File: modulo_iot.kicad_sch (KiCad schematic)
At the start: 13 parts, among them J3 SMA_CONNECTOR, U6 BG95-M3

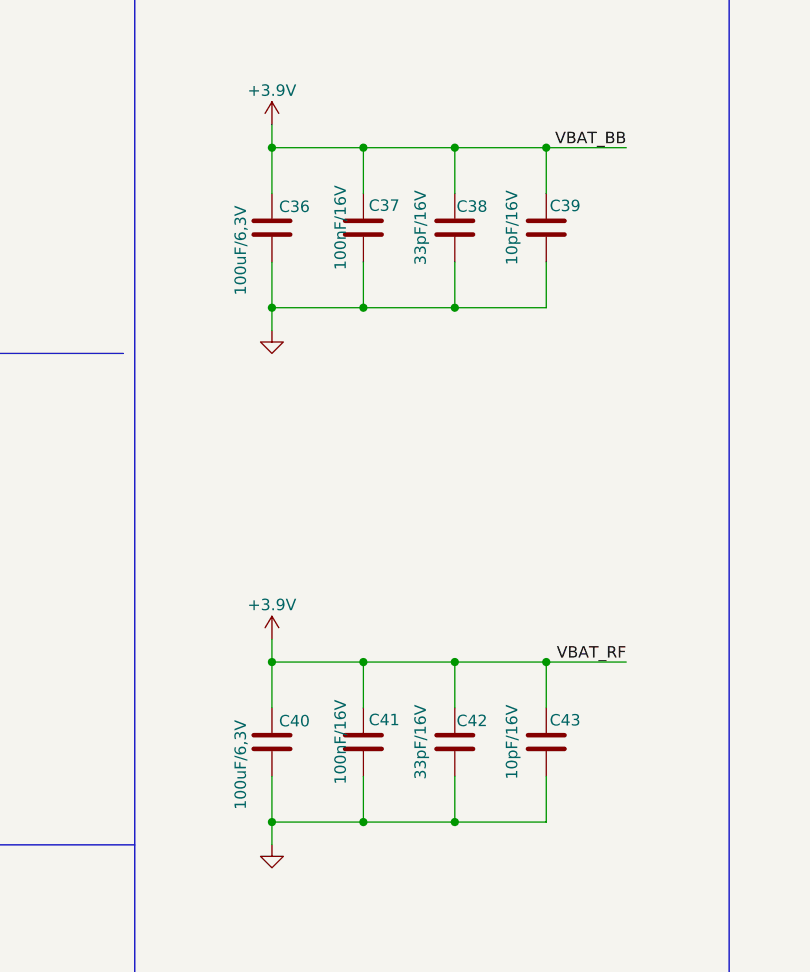
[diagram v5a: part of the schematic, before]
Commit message: Capacitores com encapsulamento 0603
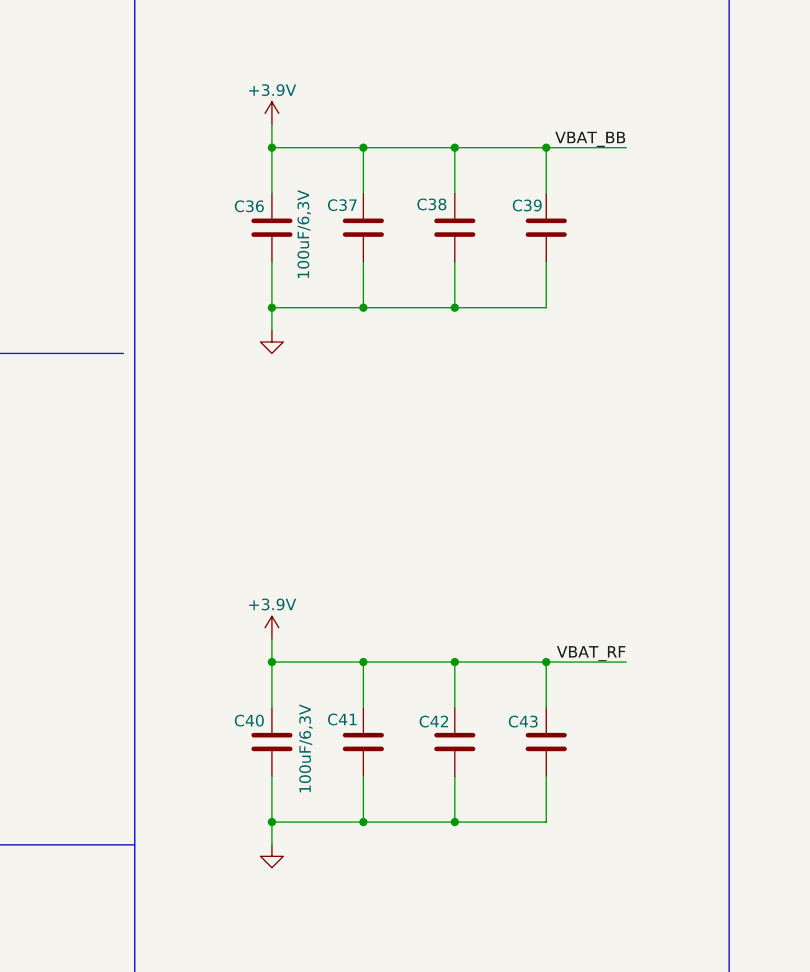
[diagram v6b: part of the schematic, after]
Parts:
- C37, C41: value 100nF/16V -> (none); footprint Capacitor_SMD:C_0402_1005Metric_Pad0.74x0.62mm_HandSolder -> (none)
- C38, C42: value 33pF/16V -> (none); footprint Capacitor_SMD:C_0402_1005Metric_Pad0.74x0.62mm_HandSolder -> (none)
- C39, C43: value 10pF/16V -> (none); footprint Capacitor_SMD:C_0402_1005Metric_Pad0.74x0.62mm_HandSolder -> (none)
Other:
- moved on the sheet: C37, C38, C39, C41, C42, C43
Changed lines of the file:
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@@
     (pin "1")
   )
-  (symbol (lib_id "Device:C") (at 146.05 115.57 180) (unit 1)
-    (in_bom yes) (on_board yes)
-    (property "Reference" "C42" (id 0) (at 147.9597 113.2135 0))
-    (property "Value" "33pF/16V" (id 1) (at 142.24 115.57 90))
-    (property "Footprint" "Capacitor_SMD:C_0402_1005Metric_Pad0.74x0.62mm_HandSolder" (id 2) (at 145.0848 111.76 0)
+  (symbol (lib_id "Device:C") (at 146.05 115.57 0) (mirror x) (unit 1)
+    (in_bom yes) (on_board yes)
+    (property "Reference" "C42" (id 0) (at 143.7582 113.3423 0))
+    (property "Value" "" (id 1) (at 149.543 115.6308 90))
+    (property "Footprint" "" (id 2) (at 147.0152 111.76 0)
       (effects (font (size 1.27 1.27)) hide)
     )
@@
     (pin "2")
   )
-  (symbol (lib_id "Device:C") (at 125.73 58.42 0) (unit 1)
-    (in_bom yes) (on_board yes)
-    (property "Reference" "C36" (id 0) (at 126.5155 56.0886 0)
+  (symbol (lib_id "Device:C") (at 125.73 58.42 0) (mirror y) (unit 1)
+    (in_bom yes) (on_board yes)
+    (property "Reference" "C36" (id 0) (at 124.9445 56.0886 0)
       (effects (font (size 1.27 1.27)) (justify left))
     )
-    (property "Value" "100uF/6,3V" (id 1) (at 122.2519 65.9392 90)
+    (property "Value" "100uF/6,3V" (id 1) (at 129.2704 64.2006 90)
       (effects (font (size 1.27 1.27)) (justify left))
     )
-    (property "Footprint" "Capacitor_SMD:C_1206_3216Metric_Pad1.33x1.80mm_HandSolder" (id 2) (at 126.6952 62.23 0)
+    (property "Footprint" "Capacitor_SMD:C_1206_3216Metric_Pad1.33x1.80mm_HandSolder" (id 2) (at 124.7648 62.23 0)
       (effects (font (size 1.27 1.27)) hide)
     )
@@
     (pin "2")
   )
-  (symbol (lib_id "Device:C") (at 125.73 115.57 0) (unit 1)
-    (in_bom yes) (on_board yes)
-    (property "Reference" "C40" (id 0) (at 126.5155 113.2386 0)
+  (symbol (lib_id "Device:C") (at 125.73 115.57 0) (mirror y) (unit 1)
+    (in_bom yes) (on_board yes)
+    (property "Reference" "C40" (id 0) (at 124.9445 113.2386 0)
       (effects (font (size 1.27 1.27)) (justify left))
     )
-    (property "Value" "100uF/6,3V" (id 1) (at 122.2519 123.0892 90)
+    (property "Value" "100uF/6,3V" (id 1) (at 129.4653 121.352 90)
       (effects (font (size 1.27 1.27)) (justify left))
     )
-    (property "Footprint" "Capacitor_SMD:C_1206_3216Metric_Pad1.33x1.80mm_HandSolder" (id 2) (at 126.6952 119.38 0)
+    (property "Footprint" "Capacitor_SMD:C_1206_3216Metric_Pad1.33x1.80mm_HandSolder" (id 2) (at 124.7648 119.38 0)
       (effects (font (size 1.27 1.27)) hide)
     )
@@
     (pin "2")
   )
-  (symbol (lib_id "Device:C") (at 156.21 58.42 180) (unit 1)
-    (in_bom yes) (on_board yes)
-    (property "Reference" "C39" (id 0) (at 158.3076 55.9943 0))
-    (property "Value" "10pF/16V" (id 1) (at 152.4 58.42 90))
-    (property "Footprint" "Capacitor_SMD:C_0402_1005Metric_Pad0.74x0.62mm_HandSolder" (id 2) (at 155.2448 54.61 0)
+  (symbol (lib_id "Device:C") (at 156.21 58.42 0) (mirror x) (unit 1)
+    (in_bom yes) (on_board yes)
+    (property "Reference" "C39" (id 0) (at 154.1124 55.9943 0))
+    (property "Value" "" (id 1) (at 159.5928 58.4158 90))
+    (property "Footprint" "" (id 2) (at 157.1752 54.61 0)
       (effects (font (size 1.27 1.27)) hide)
     )
@@
     (pin "1")
   )
-  (symbol (lib_id "Device:C") (at 135.89 58.42 180) (unit 1)
-    (in_bom yes) (on_board yes)
-    (property "Reference" "C37" (id 0) (at 138.2001 55.9597 0))
-    (property "Value" "100nF/16V" (id 1) (at 133.35 58.42 90))
-    (property "Footprint" "Capacitor_SMD:C_0402_1005Metric_Pad0.74x0.62mm_HandSolder" (id 2) (at 134.9248 54.61 0)
+  (symbol (lib_id "Device:C") (at 135.89 58.42 0) (mirror x) (unit 1)
+    (in_bom yes) (on_board yes)
+    (property "Reference" "C37" (id 0) (at 133.5799 55.9597 0))
+    (property "Value" "" (id 1) (at 139.4414 58.5429 90))
+    (property "Footprint" "" (id 2) (at 136.8552 54.61 0)
       (effects (font (size 1.27 1.27)) hide)
     )
@@
     (pin "2")
   )
-  (symbol (lib_id "Device:C") (at 156.21 115.57 180) (unit 1)
-    (in_bom yes) (on_board yes)
-    (property "Reference" "C43" (id 0) (at 158.3076 113.1443 0))
-    (property "Value" "10pF/16V" (id 1) (at 152.4 115.57 90))
-    (property "Footprint" "Capacitor_SMD:C_0402_1005Metric_Pad0.74x0.62mm_HandSolder" (id 2) (at 155.2448 111.76 0)
+  (symbol (lib_id "Device:C") (at 156.21 115.57 0) (mirror x) (unit 1)
+    (in_bom yes) (on_board yes)
+    (property "Reference" "C43" (id 0) (at 153.675 113.3423 0))
+    (property "Value" "" (id 1) (at 159.5233 115.6308 90))
+    (property "Footprint" "" (id 2) (at 157.1752 111.76 0)
       (effects (font (size 1.27 1.27)) hide)
     )
@@
     (pin "1")
   )
-  (symbol (lib_id "Device:C") (at 146.05 58.42 180) (unit 1)
-    (in_bom yes) (on_board yes)
-    (property "Reference" "C38" (id 0) (at 147.9597 56.0635 0))
-    (property "Value" "33pF/16V" (id 1) (at 142.24 58.42 90))
-    (property "Footprint" "Capacitor_SMD:C_0402_1005Metric_Pad0.74x0.62mm_HandSolder" (id 2) (at 145.0848 54.61 0)
+  (symbol (lib_id "Device:C") (at 146.05 58.42 0) (mirror x) (unit 1)
+    (in_bom yes) (on_board yes)
+    (property "Reference" "C38" (id 0) (at 143.51 55.88 0))
+    (property "Value" "" (id 1) (at 149.4853 58.5429 90))
+    (property "Footprint" "" (id 2) (at 147.0152 54.61 0)
       (effects (font (size 1.27 1.27)) hide)
     )
@@
     (pin "2")
   )
-  (symbol (lib_id "Device:C") (at 135.89 115.57 180) (unit 1)
-    (in_bom yes) (on_board yes)
-    (property "Reference" "C41" (id 0) (at 138.2001 113.1097 0))
-    (property "Value" "100nF/16V" (id 1) (at 133.35 115.57 90))
-    (property "Footprint" "Capacitor_SMD:C_0402_1005Metric_Pad0.74x0.62mm_HandSolder" (id 2) (at 134.9248 111.76 0)
-      (effects (font (size 1.27 1.27)) hide)
-    )
+  (symbol (lib_id "Device:C") (at 135.89 115.57 0) (mirror x) (unit 1)
+    (in_bom yes) (on_board yes)
+    (property "Reference" "C41" (id 0) (at 133.5799 113.1097 0))
+    (property "Value" "" (id 1) (at 139.1177 115.6308 90))
+    (property "Footprint" "" (id 2) (at 136.8552 111.76 0)
+      (effects (font (size 1.27 1.27)) hide)
+    )

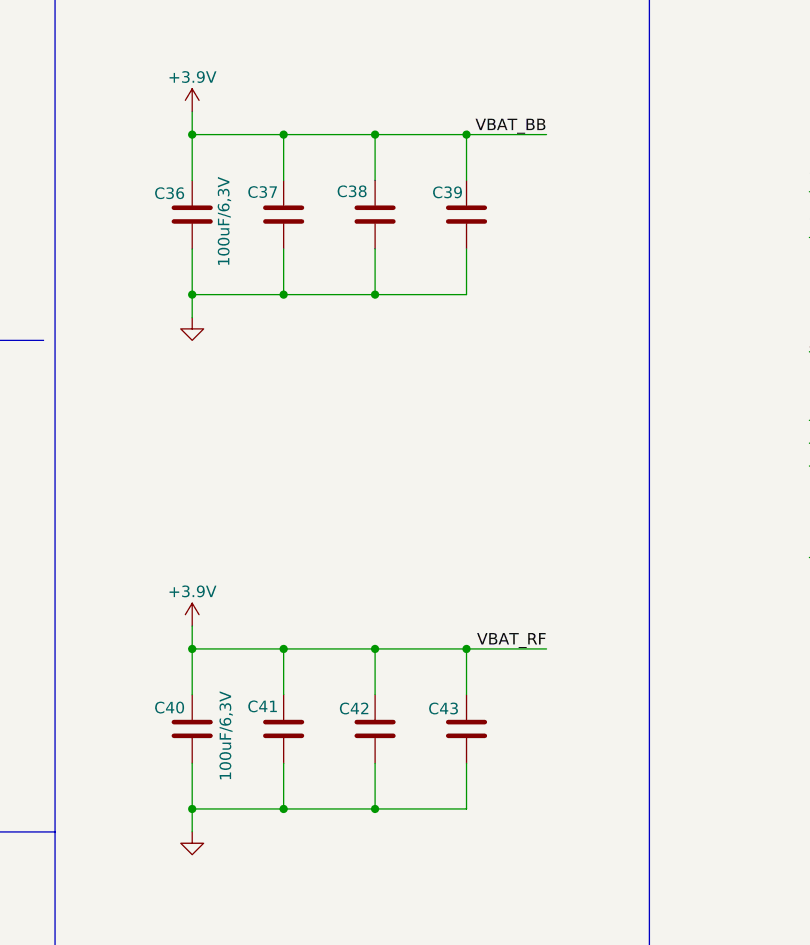
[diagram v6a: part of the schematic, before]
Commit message: Adicionado os pads dos Test Point e alterado o Bead
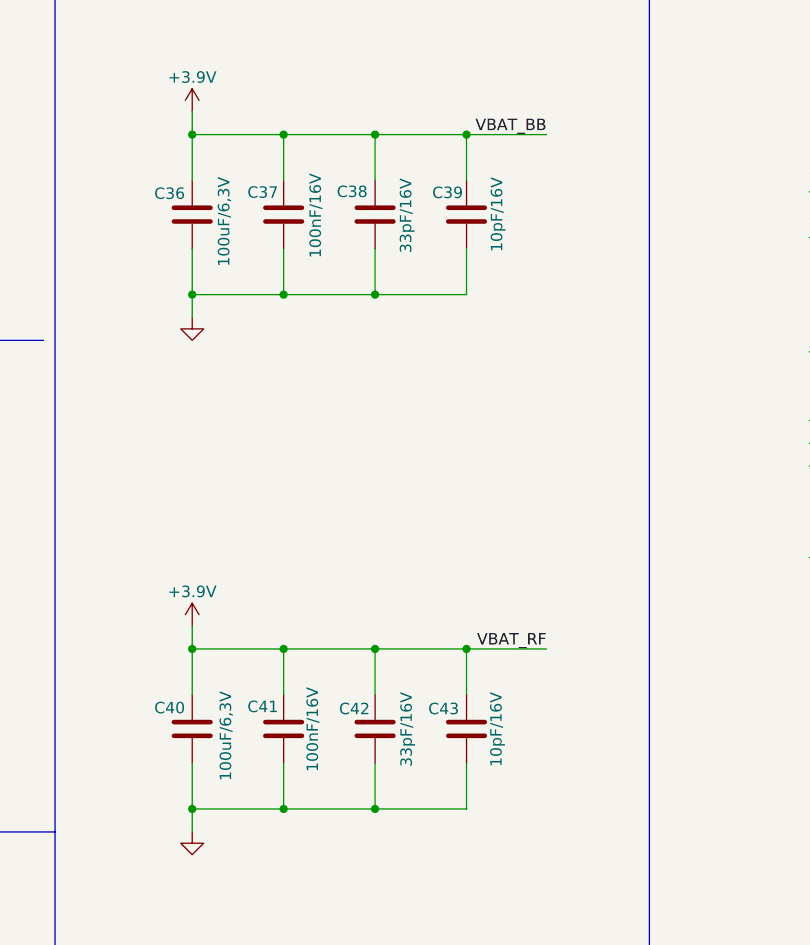
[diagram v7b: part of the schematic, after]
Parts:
- C37, C41: value (none) -> 100nF/16V; footprint (none) -> Capacitor_SMD:C_0603_1608Metric_Pad1.08x0.95mm_HandSolder
- C38, C42: value (none) -> 33pF/16V; footprint (none) -> Capacitor_SMD:C_0603_1608Metric_Pad1.08x0.95mm_HandSolder
- C39, C43: value (none) -> 10pF/16V; footprint (none) -> Capacitor_SMD:C_0603_1608Metric_Pad1.08x0.95mm_HandSolder
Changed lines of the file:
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@@
   (symbol (lib_id "Alexandre_Library:Power") (at 147.32 162.56 0) (unit 1)
     (in_bom yes) (on_board yes)
-    (property "Reference" "#PWR99" (id 0) (at 147.32 154.94 0)
+    (property "Reference" "#PWR100" (id 0) (at 147.32 154.94 0)
       (effects (font (size 1.27 1.27)) hide)
     )
@@
   (symbol (lib_id "power:GND") (at 255.27 151.13 0) (unit 1)
     (in_bom yes) (on_board yes) (fields_autoplaced)
-    (property "Reference" "#PWR097" (id 0) (at 255.27 157.48 0)
+    (property "Reference" "#PWR098" (id 0) (at 255.27 157.48 0)
       (effects (font (size 1.27 1.27)) hide)
     )
@@
   (symbol (lib_id "power:GND") (at 125.73 127 0) (mirror y) (unit 1)
     (in_bom yes) (on_board yes) (fields_autoplaced)
-    (property "Reference" "#PWR094" (id 0) (at 125.73 133.35 0)
+    (property "Reference" "#PWR095" (id 0) (at 125.73 133.35 0)
       (effects (font (size 1.27 1.27)) hide)
     )
@@
   (symbol (lib_id "power:GND") (at 139.7 170.18 0) (unit 1)
     (in_bom yes) (on_board yes) (fields_autoplaced)
-    (property "Reference" "#PWR0100" (id 0) (at 139.7 176.53 0)
+    (property "Reference" "#PWR0101" (id 0) (at 139.7 176.53 0)
       (effects (font (size 1.27 1.27)) hide)
     )
@@
   (symbol (lib_id "power:GND") (at 46.99 113.03 0) (unit 1)
     (in_bom yes) (on_board yes) (fields_autoplaced)
-    (property "Reference" "#PWR0107" (id 0) (at 46.99 119.38 0)
+    (property "Reference" "#PWR094" (id 0) (at 46.99 119.38 0)
       (effects (font (size 1.27 1.27)) hide)
     )
@@
     (in_bom yes) (on_board yes)
     (property "Reference" "C42" (id 0) (at 143.7582 113.3423 0))
-    (property "Value" "" (id 1) (at 149.543 115.6308 90))
-    (property "Footprint" "" (id 2) (at 147.0152 111.76 0)
+    (property "Value" "33pF/16V" (id 1) (at 149.543 115.6308 90))
+    (property "Footprint" "Capacitor_SMD:C_0603_1608Metric_Pad1.08x0.95mm_HandSolder" (id 2) (at 147.0152 111.76 0)
       (effects (font (size 1.27 1.27)) hide)
     )
@@
     (in_bom yes) (on_board yes)
     (property "Reference" "C39" (id 0) (at 154.1124 55.9943 0))
-    (property "Value" "" (id 1) (at 159.5928 58.4158 90))
-    (property "Footprint" "" (id 2) (at 157.1752 54.61 0)
+    (property "Value" "10pF/16V" (id 1) (at 159.5928 58.4158 90))
+    (property "Footprint" "Capacitor_SMD:C_0603_1608Metric_Pad1.08x0.95mm_HandSolder" (id 2) (at 157.1752 54.61 0)
       (effects (font (size 1.27 1.27)) hide)
     )
@@
   (symbol (lib_id "Alexandre_Library:Power") (at 93.98 148.59 0) (unit 1)
     (in_bom yes) (on_board yes)
-    (property "Reference" "#PWR95" (id 0) (at 93.98 140.97 0)
+    (property "Reference" "#PWR96" (id 0) (at 93.98 140.97 0)
       (effects (font (size 1.27 1.27)) hide)
     )
@@
   (symbol (lib_id "power:GND") (at 40.64 182.88 0) (unit 1)
     (in_bom yes) (on_board yes) (fields_autoplaced)
-    (property "Reference" "#PWR0101" (id 0) (at 40.64 189.23 0)
+    (property "Reference" "#PWR0102" (id 0) (at 40.64 189.23 0)
       (effects (font (size 1.27 1.27)) hide)
     )
@@
     (in_bom yes) (on_board yes)
     (property "Reference" "C37" (id 0) (at 133.5799 55.9597 0))
-    (property "Value" "" (id 1) (at 139.4414 58.5429 90))
-    (property "Footprint" "" (id 2) (at 136.8552 54.61 0)
+    (property "Value" "100nF/16V" (id 1) (at 139.4414 58.5429 90))
+    (property "Footprint" "Capacitor_SMD:C_0603_1608Metric_Pad1.08x0.95mm_HandSolder" (id 2) (at 136.8552 54.61 0)
       (effects (font (size 1.27 1.27)) hide)
     )
@@
     (in_bom yes) (on_board yes)
     (property "Reference" "C43" (id 0) (at 153.675 113.3423 0))
-    (property "Value" "" (id 1) (at 159.5233 115.6308 90))
-    (property "Footprint" "" (id 2) (at 157.1752 111.76 0)
+    (property "Value" "10pF/16V" (id 1) (at 159.5233 115.6308 90))
+    (property "Footprint" "Capacitor_SMD:C_0603_1608Metric_Pad1.08x0.95mm_HandSolder" (id 2) (at 157.1752 111.76 0)
       (effects (font (size 1.27 1.27)) hide)
     )
@@
   (symbol (lib_id "Alexandre_Library:Power") (at 39.37 151.13 0) (unit 1)
     (in_bom yes) (on_board yes)
-    (property "Reference" "#PWR96" (id 0) (at 39.37 143.51 0)
+    (property "Reference" "#PWR97" (id 0) (at 39.37 143.51 0)
       (effects (font (size 1.27 1.27)) hide)
     )
@@
   (symbol (lib_id "Alexandre_Library:Power") (at 139.7 162.56 0) (unit 1)
     (in_bom yes) (on_board yes)
-    (property "Reference" "#PWR98" (id 0) (at 139.7 154.94 0)
+    (property "Reference" "#PWR99" (id 0) (at 139.7 154.94 0)
       (effects (font (size 1.27 1.27)) hide)
     )
@@
     (in_bom yes) (on_board yes)
     (property "Reference" "C38" (id 0) (at 143.51 55.88 0))
-    (property "Value" "" (id 1) (at 149.4853 58.5429 90))
-    (property "Footprint" "" (id 2) (at 147.0152 54.61 0)
+    (property "Value" "33pF/16V" (id 1) (at 149.4853 58.5429 90))
+    (property "Footprint" "Capacitor_SMD:C_0603_1608Metric_Pad1.08x0.95mm_HandSolder" (id 2) (at 147.0152 54.61 0)
       (effects (font (size 1.27 1.27)) hide)
     )
@@
     (in_bom yes) (on_board yes)
     (property "Reference" "C41" (id 0) (at 133.5799 113.1097 0))
-    (property "Value" "" (id 1) (at 139.1177 115.6308 90))
-    (property "Footprint" "" (id 2) (at 136.8552 111.76 0)
-      (effects (font (size 1.27 1.27)) hide)
-    )
+    (property "Value" "100nF/16V" (id 1) (at 139.1177 115.6308 90))
+    (property "Footprint" "Capacitor_SMD:C_0603_1608Metric_Pad1.08x0.95mm_HandSolder" (id 2) (at 136.8552 111.76 0)
+      (effects (font (size 1.27 1.27)) hide)
+    )
